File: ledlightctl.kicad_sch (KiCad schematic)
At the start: 6 parts, among them U2 AL8860Q

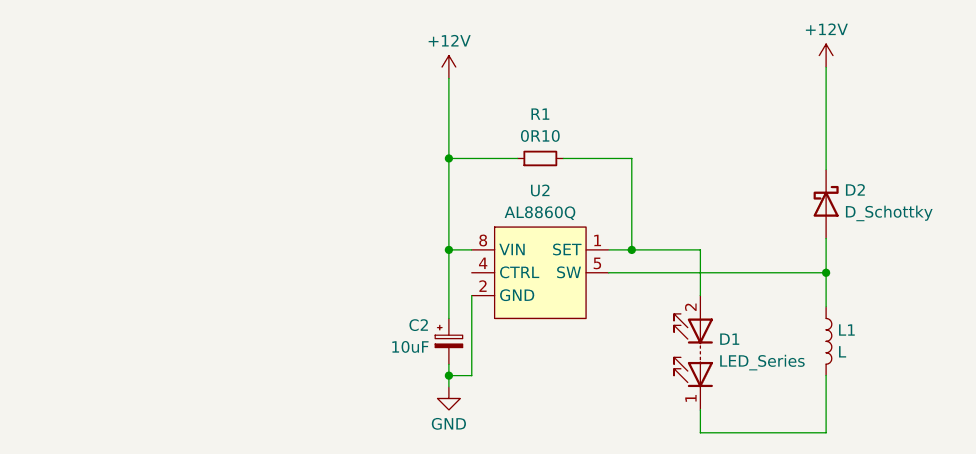
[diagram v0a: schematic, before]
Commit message: Add control pin circuit
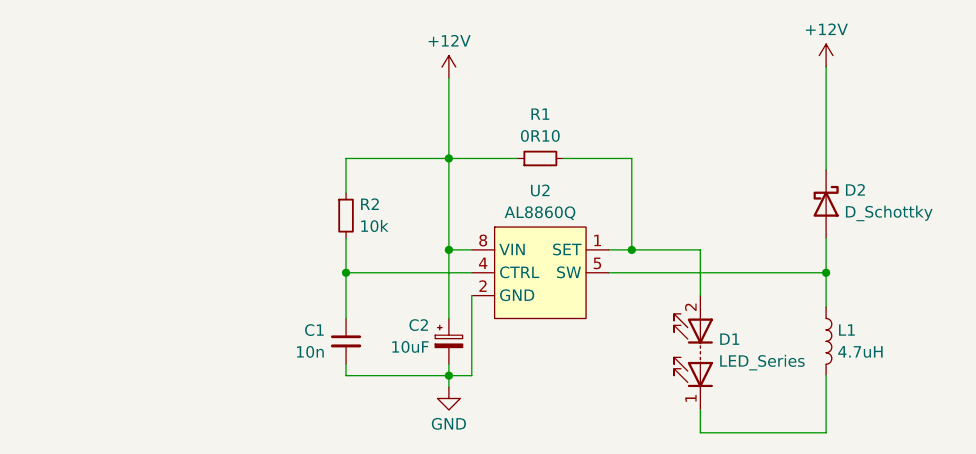
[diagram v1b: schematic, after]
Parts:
- added C1: 10n, symbol Device:C_Small
- added R2: 10k, symbol Device:R_Small
- L1: value L -> 4.7uH
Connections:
- net +12V: now also R2.1
- net GND: now also C1.2
- net at U2.4 (CTRL): now also C1.1, R2.2
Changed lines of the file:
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@@
   (junction (at 81.28 36.83) (diameter 0) (color 0 0 0 0)
   )
+  (junction (at 69.85 49.53) (diameter 0) (color 0 0 0 0)
+  )
   (junction (at 123.19 49.53) (diameter 0) (color 0 0 0 0)
   )
@@
     (stroke (width 0) (type default))
   )
+  (wire (pts (xy 69.85 40.64) (xy 69.85 36.83))
+    (stroke (width 0) (type default))
+  )
   (wire (pts (xy 109.22 64.77) (xy 109.22 67.31))
     (stroke (width 0) (type default))
@@
     (stroke (width 0) (type default))
   )
+  (wire (pts (xy 69.85 60.96) (xy 69.85 59.69))
+    (stroke (width 0) (type default))
+  )
   (wire (pts (xy 88.9 36.83) (xy 81.28 36.83))
     (stroke (width 0) (type default))
@@
     (stroke (width 0) (type default))
   )
+  (wire (pts (xy 69.85 54.61) (xy 69.85 49.53))
+    (stroke (width 0) (type default))
+  )
   (wire (pts (xy 123.19 49.53) (xy 123.19 53.34))
     (stroke (width 0) (type default))
@@
     (stroke (width 0) (type default))
   )
+  (wire (pts (xy 69.85 45.72) (xy 69.85 49.53))
+    (stroke (width 0) (type default))
+  )
+  (wire (pts (xy 81.28 60.96) (xy 69.85 60.96))
+    (stroke (width 0) (type default))
+  )
   (wire (pts (xy 81.28 27.94) (xy 81.28 36.83))
     (stroke (width 0) (type default))
@@
     (stroke (width 0) (type default))
   )
+  (wire (pts (xy 69.85 36.83) (xy 81.28 36.83))
+    (stroke (width 0) (type default))
+  )
   (wire (pts (xy 81.28 60.96) (xy 81.28 62.23))
     (stroke (width 0) (type default))
   )
+  (wire (pts (xy 69.85 49.53) (xy 83.82 49.53))
+    (stroke (width 0) (type default))
+  )
   (wire (pts (xy 99.06 49.53) (xy 123.19 49.53))
     (stroke (width 0) (type default))
@@
         (path "/f0318695-8d25-4304-9e35-c3cd5d385027"
           (reference "#PWR01") (unit 1)
+        )
+      )
+    )
+  )
+  (symbol (lib_id "Device:C_Small") (at 69.85 57.15 0) (unit 1)
+    (in_bom yes) (on_board yes) (dnp no) (fields_autoplaced)
+    (property "Reference" "C1" (at 67.5259 55.9442 0)
+      (effects (font (size 1.27 1.27)) (justify right))
+    )
+    (property "Value" "10n" (at 67.5259 58.3684 0)
+      (effects (font (size 1.27 1.27)) (justify right))
+    )
+    (property "Footprint" "" (at 69.85 57.15 0)
+      (effects (font (size 1.27 1.27)) hide)
+    )
+    (property "Datasheet" "~" (at 69.85 57.15 0)
+      (effects (font (size 1.27 1.27)) hide)
+    )
+    (pin "1")
+    (pin "2")
+    (instances
+      (project "ledlightctl"
+        (path "/f0318695-8d25-4304-9e35-c3cd5d385027"
+          (reference "C1") (unit 1)
+        )
+      )
+    )
+  )
+  (symbol (lib_id "Device:R_Small") (at 69.85 43.18 0) (unit 1)
+    (in_bom yes) (on_board yes) (dnp no) (fields_autoplaced)
+    (property "Reference" "R2" (at 71.3486 41.9679 0)
+      (effects (font (size 1.27 1.27)) (justify left))
+    )
+    (property "Value" "10k" (at 71.3486 44.3921 0)
+      (effects (font (size 1.27 1.27)) (justify left))
+    )
+    (property "Footprint" "" (at 69.85 43.18 0)
+      (effects (font (size 1.27 1.27)) hide)
+    )
+    (property "Datasheet" "~" (at 69.85 43.18 0)
+      (effects (font (size 1.27 1.27)) hide)
+    )
+    (pin "1")
+    (pin "2")
+    (instances
+      (project "ledlightctl"
+        (path "/f0318695-8d25-4304-9e35-c3cd5d385027"
+          (reference "R2") (unit 1)
         )
       )
@@
       (effects (font (size 1.27 1.27)) (justify left))
     )
-    (property "Value" "L" (at 124.4572 58.3621 0)
-      (effects (font (size 1.27 1.27)) (justify left))
-    )
+    (property "Value" "4.7uH" (at 124.4572 58.3621 0)
+      (effects (font (size 1.27 1.27)) (justify left))
+    )

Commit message: Select footprints
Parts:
- C1: footprint (none) -> Capacitor_SMD:C_0805_2012Metric_Pad1.18x1.45mm_HandSolder
- C2: footprint (none) -> Capacitor_SMD:CP_Elec_4x3
- D1: footprint (none) -> Connector_Phoenix_MC:PhoenixContact_MCV_1,5_2-G-3.5_1x02_P3.50mm_Vertical
- D2: footprint (none) -> Diode_SMD:D_0805_2012Metric_Pad1.15x1.40mm_HandSolder
- L1: footprint (none) -> Inductor_SMD:L_Coilcraft_XAL4020-XXX
- R1, R2: footprint (none) -> Resistor_SMD:R_0805_2012Metric_Pad1.20x1.40mm_HandSolder
- U2: footprint (none) -> Package_SO:SSOP-8_3.9x5.05mm_P1.27mm
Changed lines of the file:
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@@
       (effects (font (size 1.27 1.27)) (justify right))
     )
-    (property "Footprint" "" (at 69.85 57.15 0)
+    (property "Footprint" "Capacitor_SMD:C_0805_2012Metric_Pad1.18x1.45mm_HandSolder" (at 69.85 57.15 0)
       (effects (font (size 1.27 1.27)) hide)
     )
@@
       (effects (font (size 1.27 1.27)) (justify left))
     )
-    (property "Footprint" "" (at 69.85 43.18 0)
+    (property "Footprint" "Resistor_SMD:R_0805_2012Metric_Pad1.20x1.40mm_HandSolder" (at 69.85 43.18 0)
       (effects (font (size 1.27 1.27)) hide)
     )
@@
       (effects (font (size 1.27 1.27)))
     )
-    (property "Footprint" "" (at 86.36 46.99 0)
+    (property "Footprint" "Package_SO:SSOP-8_3.9x5.05mm_P1.27mm" (at 86.36 46.99 0)
       (effects (font (size 1.27 1.27)) hide)
     )
@@
       (effects (font (size 1.27 1.27)) (justify right))
     )
-    (property "Footprint" "" (at 109.22 60.96 0)
+    (property "Footprint" "Connector_Phoenix_MC:PhoenixContact_MCV_1,5_2-G-3.5_1x02_P3.50mm_Vertical" (at 109.22 60.96 0)
       (effects (font (size 1.27 1.27)) hide)
     )
@@
       (effects (font (size 1.27 1.27)) (justify right))
     )
-    (property "Footprint" "" (at 81.28 57.15 0)
+    (property "Footprint" "Capacitor_SMD:CP_Elec_4x3" (at 81.28 57.15 0)
       (effects (font (size 1.27 1.27)) hide)
     )
@@
       (effects (font (size 1.27 1.27)) (justify left))
     )
-    (property "Footprint" "" (at 123.19 57.15 0)
+    (property "Footprint" "Inductor_SMD:L_Coilcraft_XAL4020-XXX" (at 123.19 57.15 0)
       (effects (font (size 1.27 1.27)) hide)
     )
@@
       (effects (font (size 1.27 1.27)))
     )
-    (property "Footprint" "" (at 91.44 36.83 0)
+    (property "Footprint" "Resistor_SMD:R_0805_2012Metric_Pad1.20x1.40mm_HandSolder" (at 91.44 36.83 0)
       (effects (font (size 1.27 1.27)) hide)
     )
@@
       (effects (font (size 1.27 1.27)) (justify left))
     )
-    (property "Footprint" "" (at 123.19 41.91 0)
-      (effects (font (size 1.27 1.27)) hide)
-    )
+    (property "Footprint" "Diode_SMD:D_0805_2012Metric_Pad1.15x1.40mm_HandSolder" (at 123.19 41.91 0)
+      (effects (font (size 1.27 1.27)) hide)
+    )

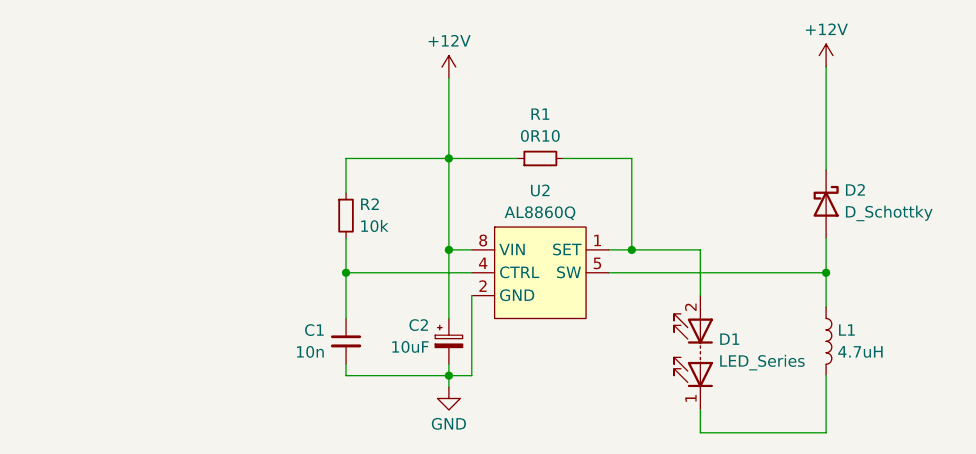
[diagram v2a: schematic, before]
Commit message: Add power connector Add copper zones
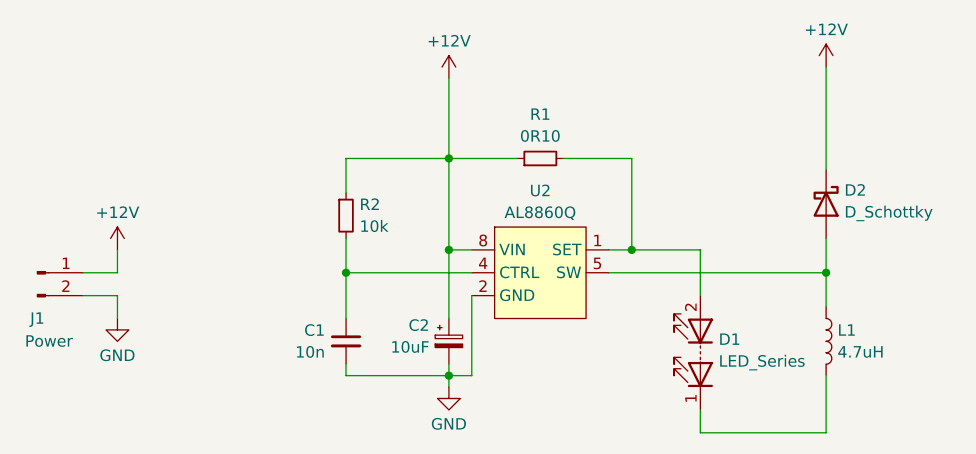
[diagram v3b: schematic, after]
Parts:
- added J1: Power, Connector_Phoenix_MC:PhoenixContact_MCV_1,5_2-G-3.5_1x02_P3.50mm_Vertical, symbol Connector:Conn_01x02_Pin
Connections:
- net +12V: now also J1.1 (Pin_1)
- net GND: now also J1.2 (Pin_2)
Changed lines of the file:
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@@
+    (stroke (width 0) (type default))
+  )
+  (wire (pts (xy 44.45 54.61) (xy 44.45 52.07))
     (stroke (width 0) (type default))
   )
@@
     (stroke (width 0) (type default))
   )
+  (wire (pts (xy 44.45 49.53) (xy 40.64 49.53))
+    (stroke (width 0) (type default))
+  )
   (wire (pts (xy 101.6 36.83) (xy 101.6 46.99))
     (stroke (width 0) (type default))
@@
     (stroke (width 0) (type default))
   )
+  (wire (pts (xy 44.45 52.07) (xy 40.64 52.07))
+    (stroke (width 0) (type default))
+  )
   (wire (pts (xy 69.85 36.83) (xy 81.28 36.83))
     (stroke (width 0) (type default))
@@
   )
   (wire (pts (xy 99.06 49.53) (xy 123.19 49.53))
+    (stroke (width 0) (type default))
+  )
+  (wire (pts (xy 44.45 46.99) (xy 44.45 49.53))
     (stroke (width 0) (type default))
   )
@@
     )
   )
+  (symbol (lib_id "power:+12V") (at 44.45 46.99 0) (unit 1)
+    (in_bom yes) (on_board yes) (dnp no) (fields_autoplaced)
+    (property "Reference" "#PWR0101" (at 44.45 50.8 0)
+      (effects (font (size 1.27 1.27)) hide)
+    )
+    (property "Value" "+12V" (at 44.45 42.8569 0)
+      (effects (font (size 1.27 1.27)))
+    )
+    (property "Footprint" "" (at 44.45 46.99 0)
+      (effects (font (size 1.27 1.27)) hide)
+    )
+    (property "Datasheet" "" (at 44.45 46.99 0)
+      (effects (font (size 1.27 1.27)) hide)
+    )
+    (pin "1")
+    (instances
+      (project "ledlightctl"
+        (path "/f0318695-8d25-4304-9e35-c3cd5d385027"
+          (reference "#PWR0101") (unit 1)
+        )
+      )
+    )
+  )
   (symbol (lib_id "Device:LED_Series") (at 109.22 58.42 90) (unit 1)
     (in_bom yes) (on_board yes) (dnp no) (fields_autoplaced)
@@
     )
   )
+  (symbol (lib_id "Connector:Conn_01x02_Pin") (at 35.56 49.53 0) (unit 1)
+    (in_bom yes) (on_board yes) (dnp no)
+    (property "Reference" "J1" (at 35.56 54.61 0)
+      (effects (font (size 1.27 1.27)))
+    )
+    (property "Value" "Power" (at 36.83 57.15 0)
+      (effects (font (size 1.27 1.27)))
+    )
+    (property "Footprint" "Connector_Phoenix_MC:PhoenixContact_MCV_1,5_2-G-3.5_1x02_P3.50mm_Vertical" (at 35.56 49.53 0)
+      (effects (font (size 1.27 1.27)) hide)
+    )
+    (property "Datasheet" "~" (at 35.56 49.53 0)
+      (effects (font (size 1.27 1.27)) hide)
+    )
+    (pin "2")
+    (pin "1")
+    (instances
+      (project "ledlightctl"
+        (path "/f0318695-8d25-4304-9e35-c3cd5d385027"
+          (reference "J1") (unit 1)
+        )
+      )
+    )
+  )
   (symbol (lib_id "Device:D_Schottky") (at 123.19 41.91 270) (unit 1)
     (in_bom yes) (on_board yes) (dnp no) (fields_autoplaced)
@@
         )
       )
+    )
+  )
+  (symbol (lib_id "power:GND") (at 44.45 54.61 0) (unit 1)
+    (in_bom yes) (on_board yes) (dnp no)
+    (property "Reference" "#PWR0102" (at 44.45 60.96 0)
+      (effects (font (size 1.27 1.27)) hide)
+    )
+    (property "Value" "GND" (at 44.45 58.7431 0)
+      (effects (font (size 1.27 1.27)))
+    )
+    (property "Footprint" "" (at 44.45 54.61 0)
+      (effects (font (size 1.27 1.27)) hide)
+    )
+    (property "Datasheet" "" (at 44.45 54.61 0)
+      (effects (font (size 1.27 1.27)) hide)
+    )
+    (pin "1")
+    (instances
+      (project "ledlightctl"
+        (path "/f0318695-8d25-4304-9e35-c3cd5d385027"
+          (reference "#PWR0102") (unit 1)
+        )
+      )
